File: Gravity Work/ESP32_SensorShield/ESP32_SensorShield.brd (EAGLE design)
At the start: 50.8 x 22.9 mm, 28 parts, among them IC1 BMP388, U1 FGPMMOPA6H, Y1 32.768kHz

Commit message: V1 dev
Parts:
- added J1, J2: (no value), SparkFun-Connectors:1X04_1MM_RA
- added J3: (no value), SparkFun-Connectors:JST-2-SMD
- added U2: MB85RC256VPF-G-JNERE2, microbuilder:SOIC8_208MIL
- moved D2 5.48 mm to (33.7, 19.9)
- moved C3 1.55 mm to (36.7, 13.3), turned to 0 degrees
- moved B1 0.36 mm to (43.4, 11.9), flipped to the bottom, turned to 90 degrees
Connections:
- new net VCC: U2.8
- net GND: now also U2.4
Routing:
- net N$7: track 23.6 -> 30.2 mm, vias 0 -> 1
- net N$6: track 34.2 -> 28.5 mm

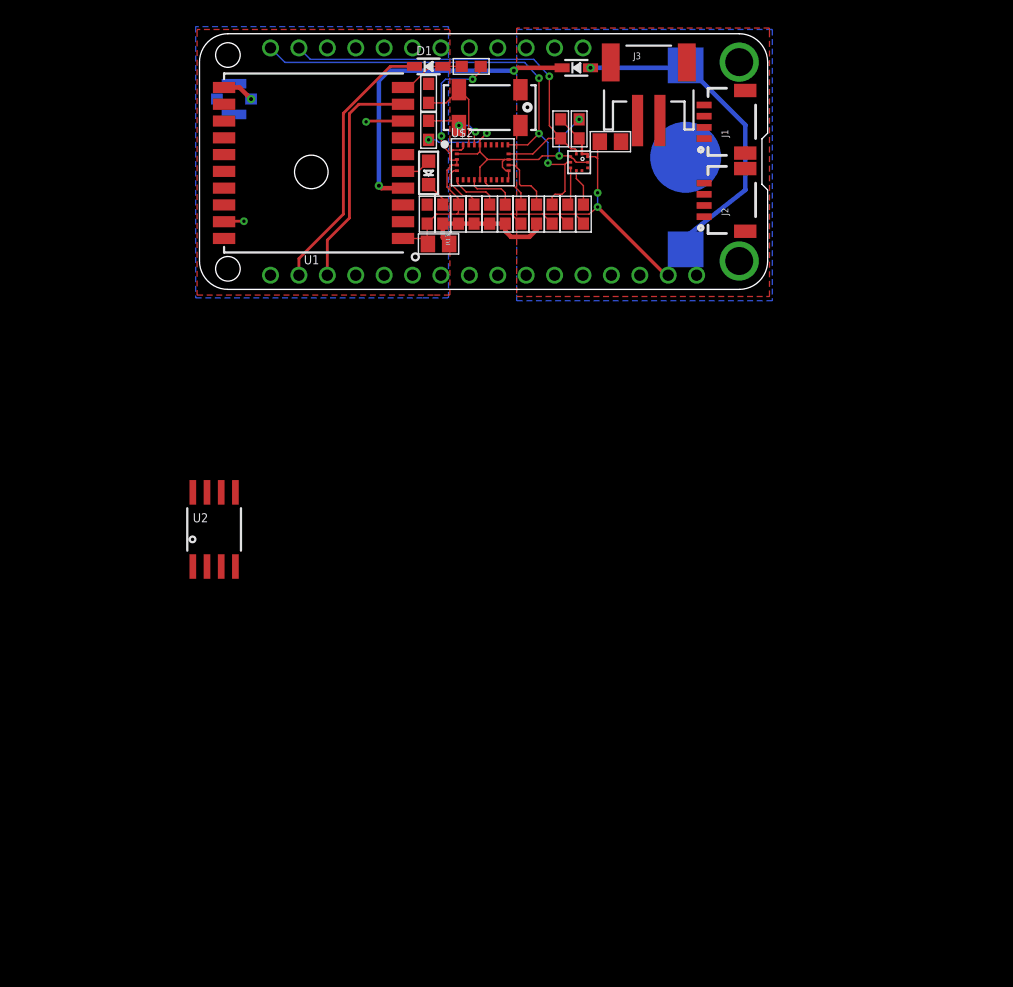
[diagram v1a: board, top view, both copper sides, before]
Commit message: Added DC2DC Conv, EEPROM, Got rid of Coin Cell, Added Switch
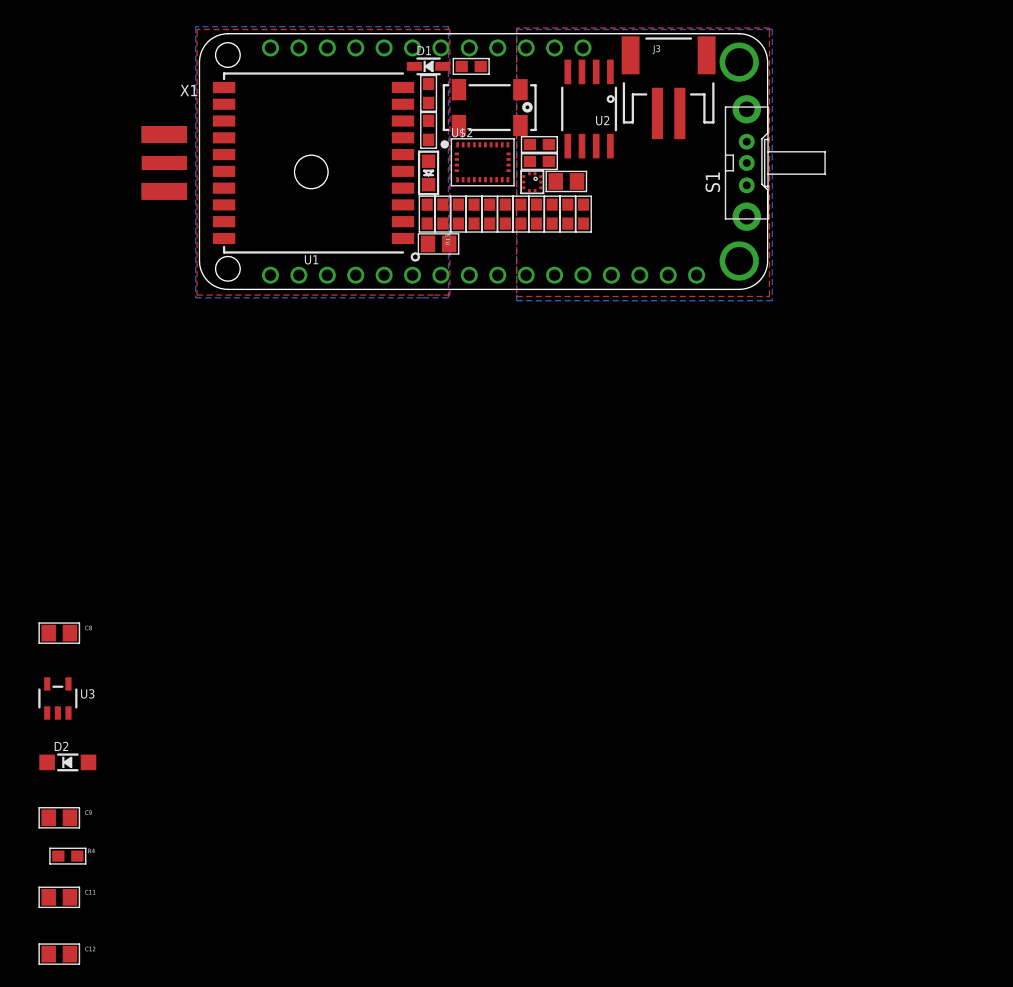
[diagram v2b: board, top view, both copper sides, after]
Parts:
- removed B1: CR1220, microbuilder:CR1220
- removed J1, J2: (no value), SparkFun-Connectors:1X04_1MM_RA
- removed U$45: U.FL, microbuilder:U.FL
- added C11, C12, C8, C9: 10uF, microbuilder:0805
- added R4: 10K, microbuilder:0603
- added S1: EG1213, adafruit:EG1213
- added U3: SPX3819-3.3, microbuilder:SOT23-5
- added X1: (no value), adafruit:SMA_EDGELAUNCH
- D2: value CUS520 -> MBR120; device microbuilder:SOD-323 -> microbuilder:SOD-123
- moved D2 77.0 mm to (-11.8, -42.2)
- moved U2 50.4 mm to (34.8, 16.3), turned to 180 degrees
- moved C3 5.31 mm to (32.8, 9.78)
- moved C6 4.60 mm to (30.4, 11.6), turned to 0 degrees
- moved IC1 4.55 mm to (29.7, 9.72)
- moved R8 2.36 mm to (30.4, 13.1), turned to 0 degrees
- moved J3 1.89 mm to (41.9, 19.6)
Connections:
- removed net N$7: B1.+$1, B1.+$2, D2.A
- removed net VCC: U2.8
- new net AUX_3V3: C11.1, C12.1, U3.5
- new net GND1: X1.GND@4
- new net GND2: X1.GND@3
- new net N$11: R4.2, U3.3
- new net VBAT: D2.A, S1.1, U$1.17
- new net VUSB: C9.1, D2.C, R4.1, U3.1
- net 3.3V: now also C8.1, U2.8
- net GND: now also C11.2, C12.2, C8.2, C9.2, J3.1, U3.2, X1.GND@1, X1.GND@2; no longer B1.-, U$45.P$1, U$45.P$2
- net N$3: now also X1.P; no longer U$45.P$3
- net N$6: now also J3.2, S1.2; no longer D2.C, U1.P$4
- net SCL: now also U2.6
- net SDA: now also U2.5
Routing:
- net 3.3V: track 65.1 -> 0.00 mm, vias 4 -> 0
- net GND: track 45.7 -> 0.00 mm, vias 6 -> 0
- net SDA: track 42.9 -> 0.00 mm, vias 3 -> 0
- net SCL: track 36.8 -> 0.00 mm, vias 1 -> 0
- net N$7: track 30.2 -> 0.00 mm, vias 1 -> 0
- net N$6: track 28.5 -> 0.00 mm, vias 2 -> 0
- net GPS_RX: track 24.2 -> 0.00 mm
- net GPS_TX: track 20.4 -> 0.00 mm
- net N$1: track 8.50 -> 0.00 mm
- net N$5: track 6.03 -> 0.00 mm
- net N$2: track 5.81 -> 0.00 mm, vias 2 -> 0
- net I2CADDR_3V: track 5.40 -> 0.00 mm
- net NRESET_3V: track 4.87 -> 0.00 mm
- net N$4: track 4.63 -> 0.00 mm
- net PS1_3V: track 4.62 -> 0.00 mm
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
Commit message: Add Communication Pins, Need to connect headers to signals.
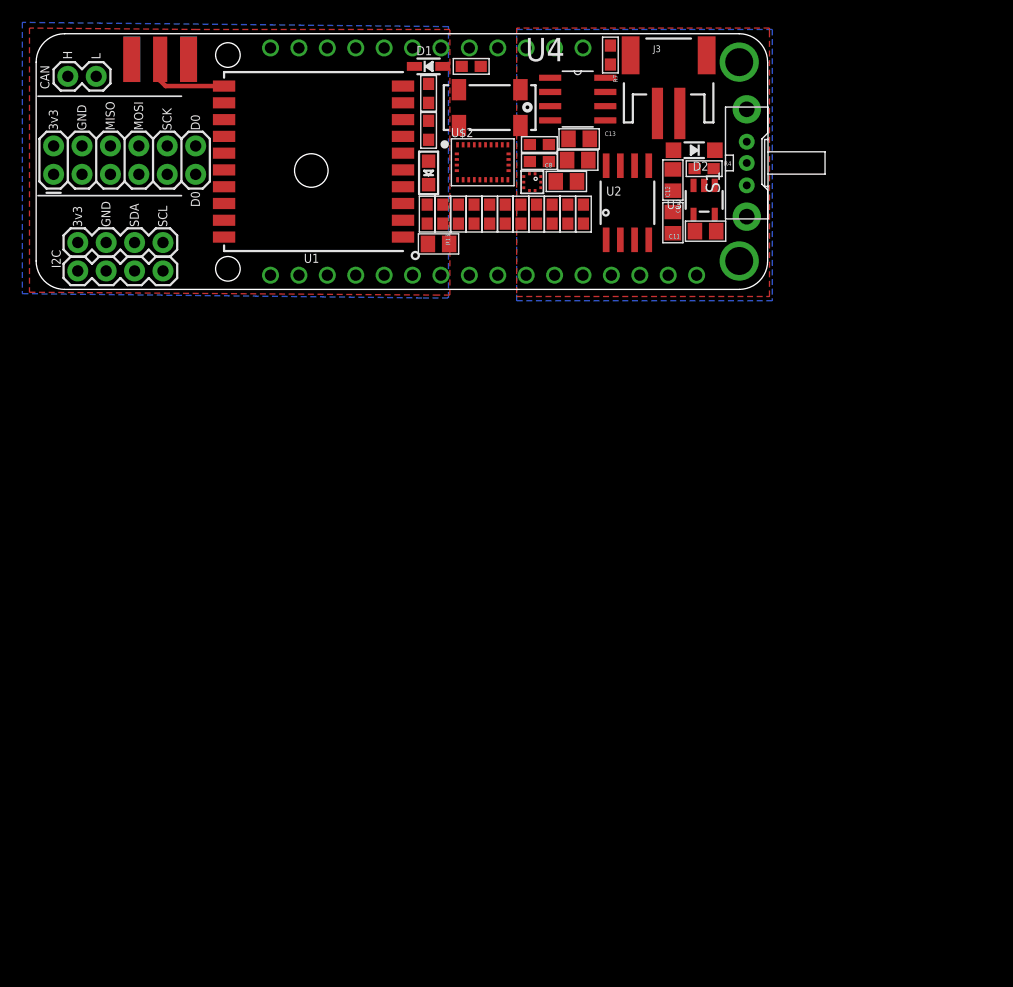
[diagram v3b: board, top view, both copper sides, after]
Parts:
- added C13: 10uF, microbuilder:0805
- added J1, J2: (no value), SparkFun-Connectors:1X04
- added J6: (no value), SparkFun-Connectors:1X02
- added J7: 2X6 FEMALE, SparkFun-Connectors:2X6
- added R7: 10k, microbuilder:0603
- added U4: SN65HVD230D, SN65HVD230D:SOIC127P600X175-8N
- C12: value 10uF -> 0.1uF
- moved C12 85.4 mm to (42.3, 6.10), turned to 90 degrees
- moved R4 83.8 mm to (45.1, 10.9)
- moved C11 83.0 mm to (45.2, 5.33), turned to 180 degrees
- moved C9 79.1 mm to (42.3, 9.91), turned to 270 degrees
- moved D2 78.3 mm to (44.2, 12.6), turned to 180 degrees
- moved U3 73.0 mm to (45.1, 8.13), turned to 180 degrees
- moved C8 62.7 mm to (33.8, 11.7), turned to 180 degrees
- moved X1 11.4 mm to (-3.56, 22.7), turned to 270 degrees
- moved U2 9.06 mm to (38.2, 7.87), turned to 0 degrees
- moved U1 0.13 mm to (10.2, 11.6)
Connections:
- new net CANH: U4.7
- new net CANL: U4.6
- new net CAN_RX: U4.4
- new net CAN_TX: U4.1
- new net GPIO36: U$1.9
- new net GPIO4: U$1.10
- new net N$10: R7.2, U4.8
- new net N$7: C13.1, U4.3
- net GND: now also C13.2, R7.1, U4.2
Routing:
- net N$3: track 0.00 -> 7.82 mm
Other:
- board size 50.8 x 22.9 mm -> 65.4 x 22.9 mm
- board text added: "3v3"
- board text added: "CAN"
- board text added: "D0"
- board text added: "GND"
- board text added: "H"
- board text added: "I2C"
- board text added: "L"
- board text added: "MISO"
- board text added: "MOSI"
- board text added: "SCK"
- board text added: "SCL"
- board text added: "SDA"

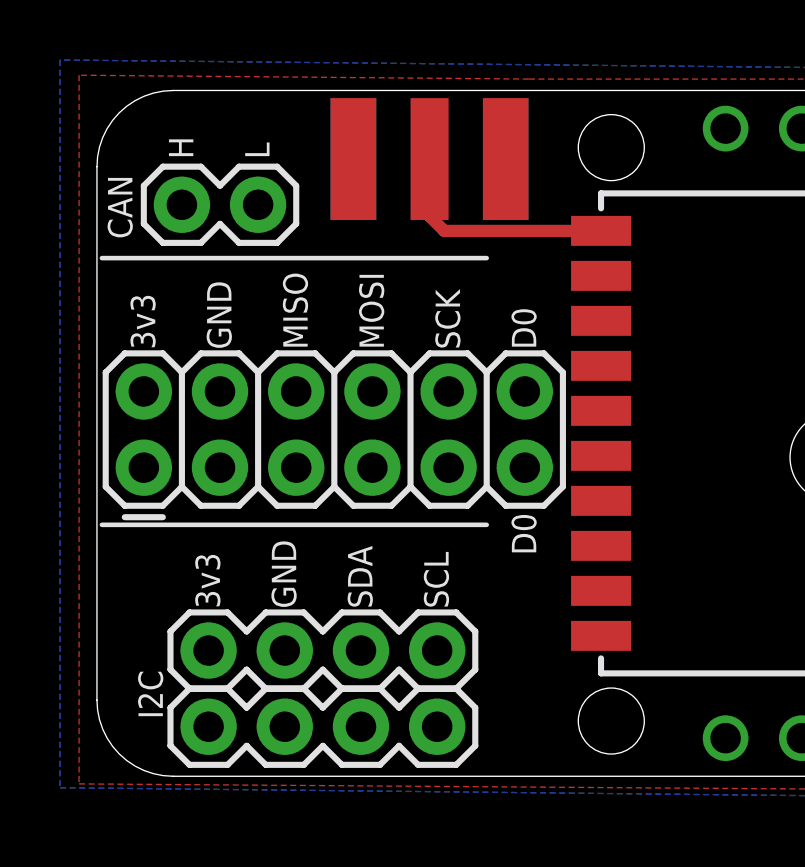
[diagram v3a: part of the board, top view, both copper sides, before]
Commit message: Moved Headers, SMA. Added LED.
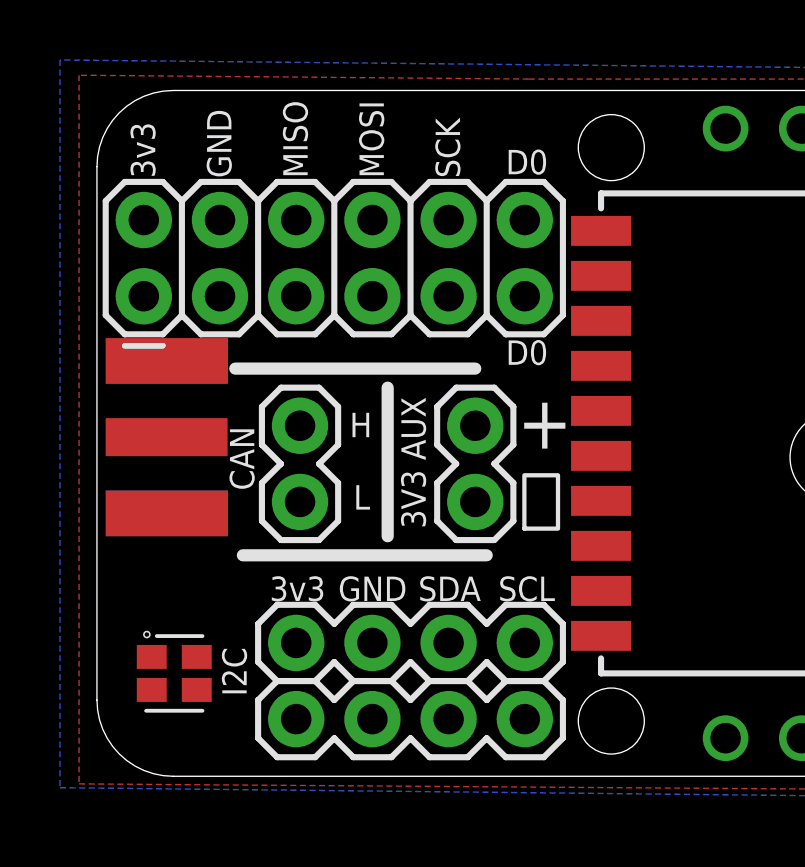
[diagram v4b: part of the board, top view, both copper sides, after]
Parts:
- added J4: (no value), SparkFun-Connectors:1X02
- added U$36: RGB-LED-CLMVB-FKARGB, Particle:PLCC4-2MM-RGB
- moved X1 15.6 mm to (-14.4, 11.4), turned to 0 degrees
- moved J6 10.0 mm to (-7.87, 9.27), turned to 90 degrees
- moved J7 5.72 mm to (-13.1, 16.1)
- moved J1 2.93 mm to (-8.00, 2.03)
- moved J2 2.93 mm to (-8.00, 4.57)
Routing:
- net N$3: track 7.82 -> 0.00 mm
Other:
- board text added: "+"
- board text added: "3V3 AUX"
- board text added: "⏚"

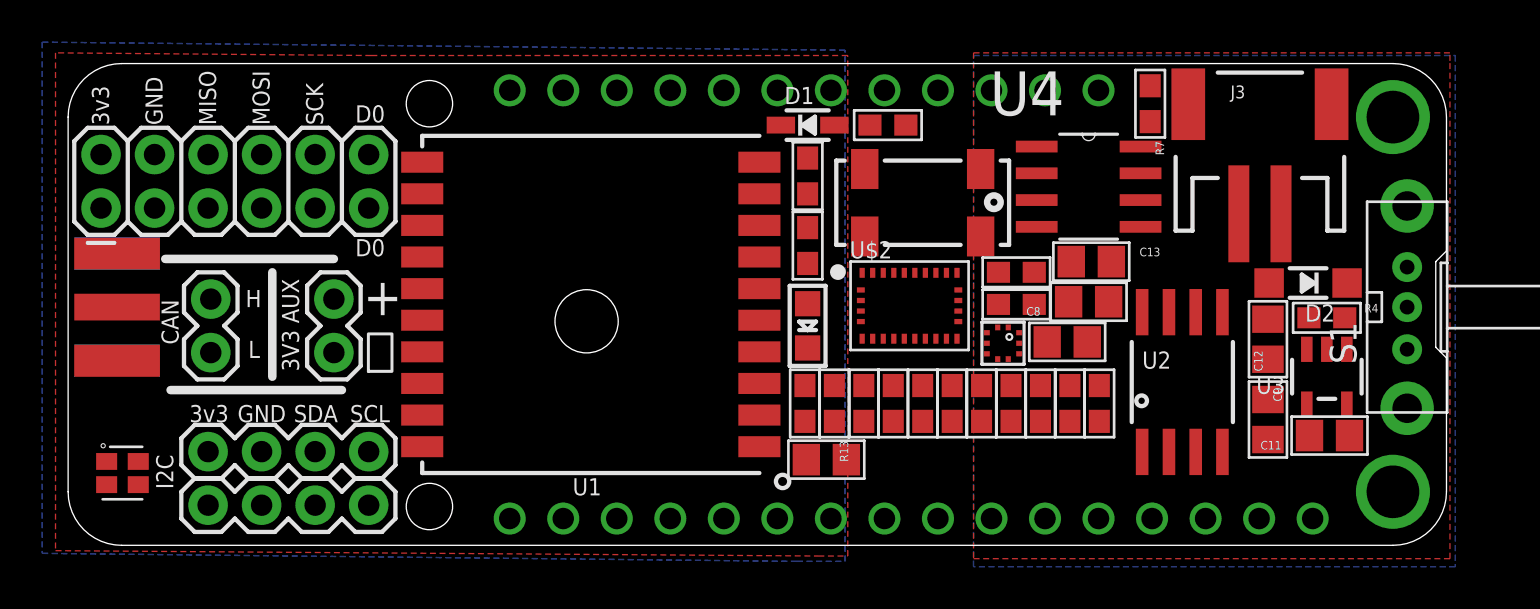
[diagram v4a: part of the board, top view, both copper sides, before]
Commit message: Moved Holes/LED around, modfied SPI Pins,began routing.
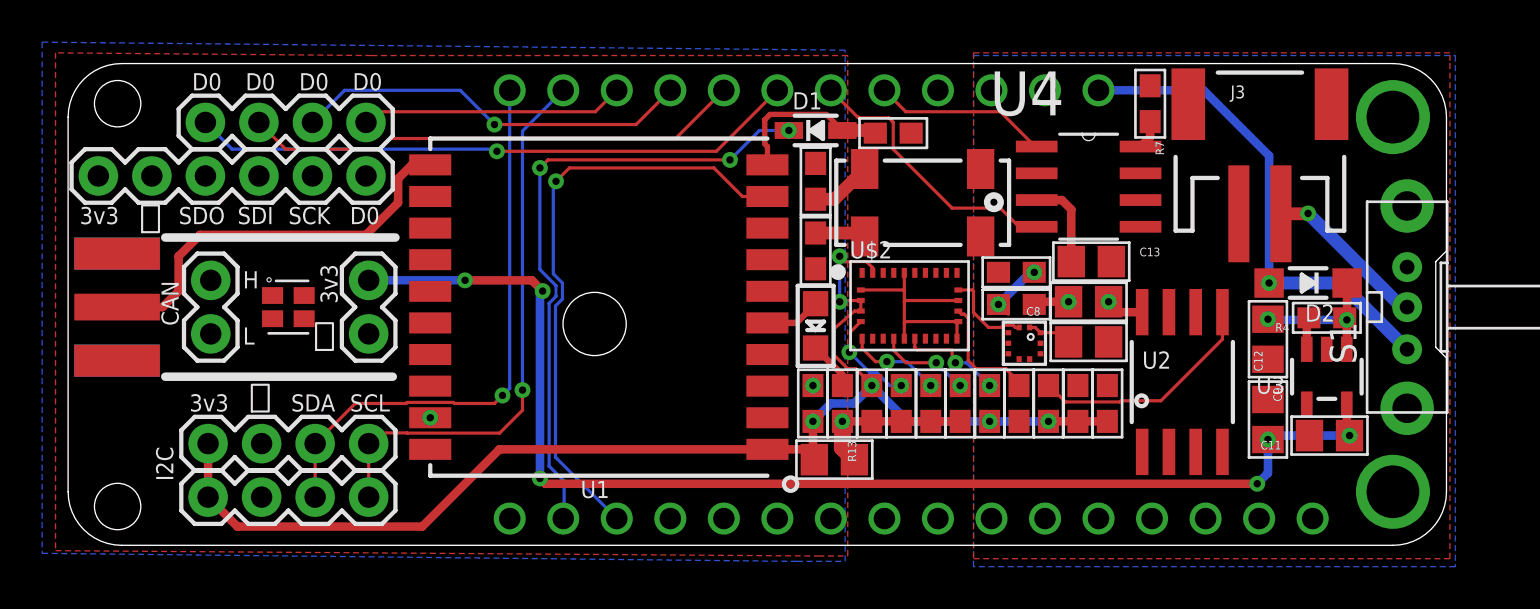
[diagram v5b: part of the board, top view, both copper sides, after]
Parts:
- removed J7: 2X6 FEMALE, SparkFun-Connectors:2X6
- added J5: (no value), SparkFun-Connectors:1X06
- added J8: (no value), SparkFun-Connectors:1X04
- moved U$36 11.1 mm to (-4.19, 11.4)
- moved J4 1.88 mm to (-0.38, 10.2)
- moved IC1 1.02 mm to (30.7, 9.72)
- moved C3 1.02 mm to (33.8, 9.78)
- moved J6 0.89 mm to (-7.87, 10.2)
- moved C2 0.46 mm to (20.8, 14.1)
- moved C1 0.46 mm to (20.8, 17.4)
- moved D1 0.46 mm to (20.8, 19.8)
- moved R10 0.46 mm to (24.5, 19.7)
- moved U1 0.40 mm to (10.5, 11.4)
- moved C10 0.38 mm to (21.7, 4.19)
- moved C4 0.38 mm to (23.5, 6.86)
- moved C5 0.38 mm to (27.7, 6.86)
- moved C7 0.38 mm to (20.7, 6.86)
- moved J2 0.38 mm to (-8.00, 4.95)
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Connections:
- removed net GPIO36: U$1.9
- removed net GPIO4: U$1.10
- new net GPIO14: J8.4, U$1.26
- new net GPIO15: J8.2, U$1.24
- new net GPIO32: J8.3, U$1.25
- new net GPIO33: J8.1, U$1.23
- net 3.3V: now also J1.1, J2.1
- net AUX_3V3: now also J4.2
- net CAN_RX: now also U$1.22
- net CAN_TX: now also U$1.21
- net GND: now also J1.2, J2.2, J4.1
- net SCL: now also J1.4, J2.4
- net SDA: now also J1.3, J2.3
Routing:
- net 3.3V: track 0.00 -> 68.6 mm, vias 0 -> 9
- net AUX_3V3: track 0.00 -> 59.4 mm, vias 0 -> 6
- net SDA: track 0.00 -> 38.1 mm, vias 0 -> 1
- net SCL: track 0.00 -> 30.8 mm, vias 0 -> 1
- net GPS_RX: track 0.00 -> 29.9 mm, vias 0 -> 3
- net GPIO33: track 0.00 -> 28.9 mm, vias 0 -> 1
- net GPS_TX: track 0.00 -> 28.4 mm, vias 0 -> 1
- net GPIO15: track 0.00 -> 23.7 mm
- net VBAT: track 0.00 -> 23.3 mm, vias 0 -> 1
- net GND: track 0.00 -> 20.6 mm, vias 0 -> 4
- net N$3: track 0.00 -> 19.3 mm
- net GPIO32: track 0.00 -> 19.0 mm, vias 0 -> 1
- net CAN_RX: track 0.00 -> 13.2 mm
- net GPIO14: track 0.00 -> 12.5 mm
- net CAN_TX: track 0.00 -> 8.33 mm
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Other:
- board text added: "SDI"
- board text added: "SDO"
- board text removed: "+"
- board text removed: "3V3 AUX"
- board text removed: "GND"
- board text removed: "MISO"
- board text removed: "MOSI"

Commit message: Completed a large portion of routing
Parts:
- removed J5: (no value), SparkFun-Connectors:1X06
- added J7: (no value), SparkFun-Connectors:1X05
- moved C6 0.13 mm to (30.4, 11.7)
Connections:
- new net MISO: J7.4, U$1.13
- new net MOSI: J7.3, U$1.12
- new net SCK: J7.5, U$1.11
- net 3.3V: now also J7.1
- net GND: now also J7.2
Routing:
- net SDA: track 38.1 -> 91.6 mm, vias 1 -> 9
- net SCL: track 30.8 -> 73.9 mm, vias 1 -> 6
- net 3.3V: track 68.6 -> 110.6 mm, vias 9 -> 14
- net MOSI: track 0.00 -> 34.1 mm, vias 0 -> 1
- net SCK: track 0.00 -> 31.6 mm, vias 0 -> 1
- net MISO: track 0.00 -> 29.6 mm, vias 0 -> 1
- net SDO/ADR: track 0.00 -> 6.81 mm, vias 0 -> 2
- net N$1: track 2.92 -> 8.22 mm
- net CS_3V: track 0.00 -> 4.76 mm
- net N$2: track 2.40 -> 6.97 mm, vias 0 -> 2
- net GND: track 20.6 -> 23.3 mm
- net N$3: track 19.3 -> 19.9 mm, vias 0 -> 2
- net N$7: track 4.30 -> 4.52 mm, vias 0 -> 2
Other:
- board text added: "14"
- board text added: "15"
- board text added: "32"
- board text added: "33"
- board text added: "MI"
- board text added: "MO"
- board text removed: "D0"
- board text removed: "SDI"
- board text removed: "SDO"
